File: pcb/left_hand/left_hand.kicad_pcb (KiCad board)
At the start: 2 copper layers, 150 x 105 mm, 43 parts, among them K0 SW_Push

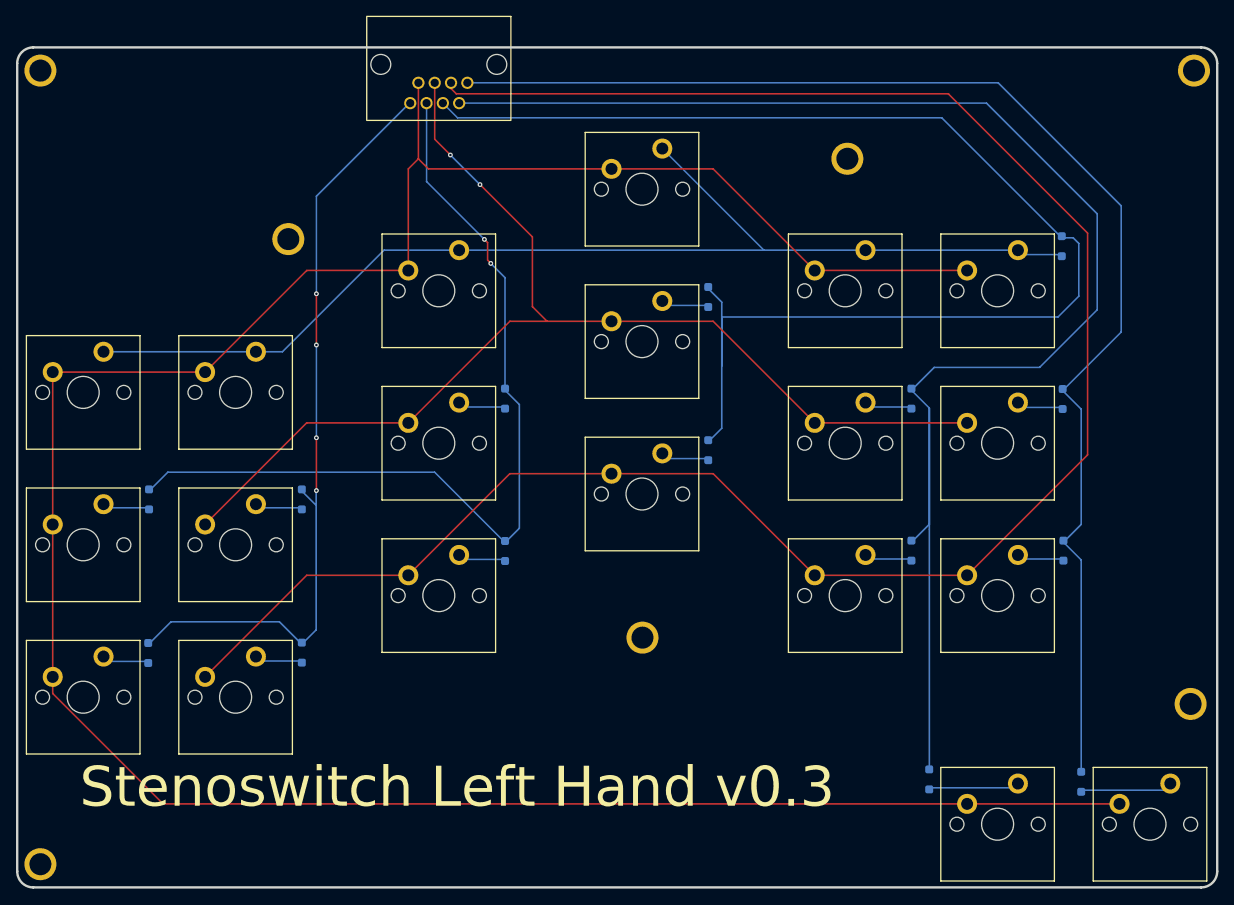
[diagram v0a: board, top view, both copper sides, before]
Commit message: Adjust left hand silkscreen; holes
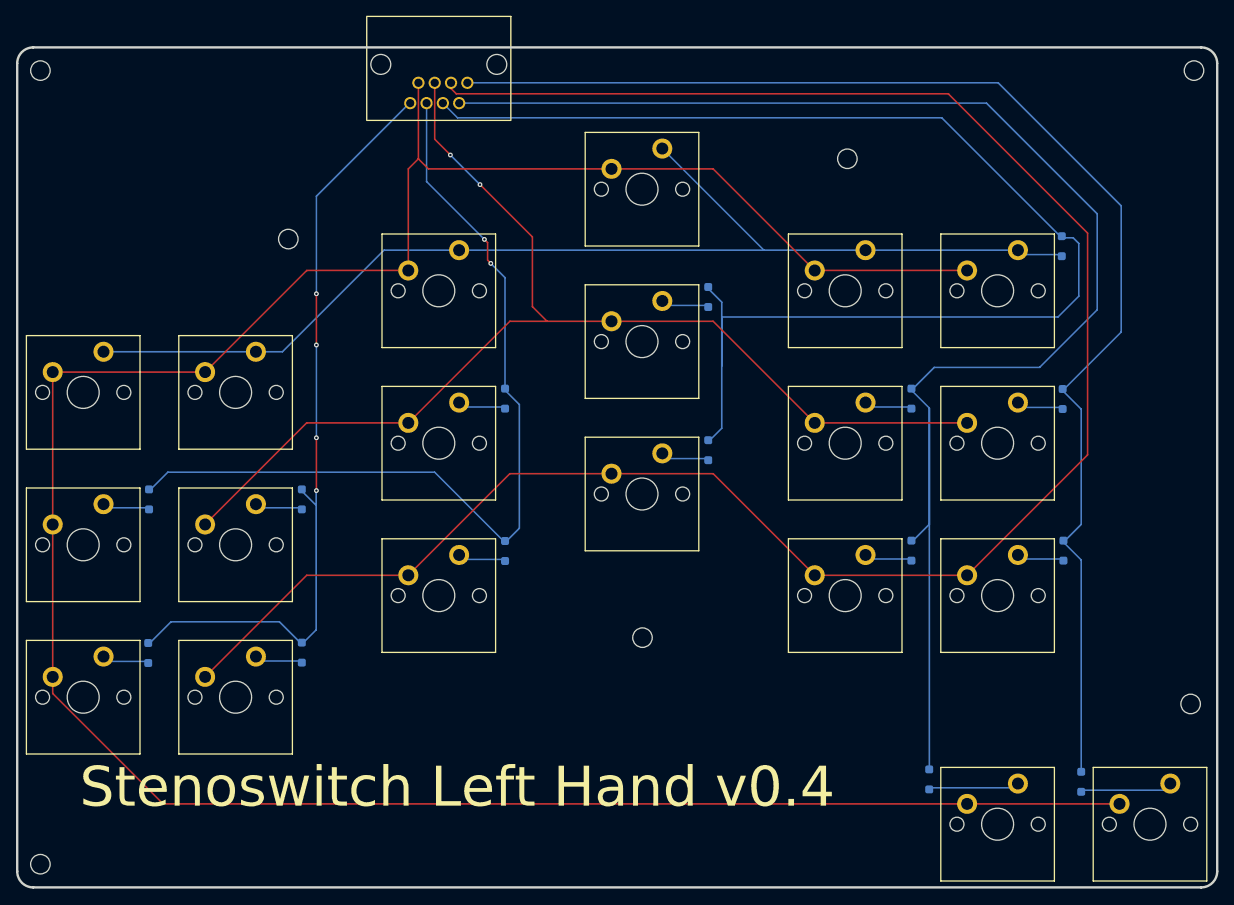
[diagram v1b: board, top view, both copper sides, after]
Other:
- board text added: "Stenoswitch Left Hand v0.4"
- board text removed: "Stenoswitch Left Hand v0.3"
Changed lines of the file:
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@@
 	(title_block
 		(title "Stenoswitch Left Hand")
-		(date "2025-10-20")
-		(rev "0.3")
+		(date "2025-11-14")
+		(rev "0.4")
 		(company "https://github.com/Bennett-Petzold/stenoswitch")
 		(comment 1 "NO WARRANTY. See license.")
@@
 			)
 		)
-		(pad "" thru_hole circle
+		(pad "" np_thru_hole circle
 			(at 0 0 180)
-			(size 4 4)
-			(drill 2.75)
+			(size 2.4384 2.4384)
+			(drill 2.4384)
 			(layers "*.Cu" "*.Mask")
-			(remove_unused_layers no)
 		)
 		(embedded_fonts no)
@@
 			)
 		)
-		(pad "" thru_hole circle
+		(pad "" np_thru_hole circle
 			(at 0 0 180)
-			(size 4 4)
-			(drill 2.75)
+			(size 2.4384 2.4384)
+			(drill 2.4384)
 			(layers "*.Cu" "*.Mask")
-			(remove_unused_layers no)
 		)
 		(embedded_fonts no)
@@
 			)
 		)
-		(pad "" thru_hole circle
+		(pad "" np_thru_hole circle
 			(at 0 0 180)
-			(size 4 4)
-			(drill 2.75)
+			(size 2.4384 2.4384)
+			(drill 2.4384)
 			(layers "*.Cu" "*.Mask")
-			(remove_unused_layers no)
 		)
 		(embedded_fonts no)
@@
 			)
 		)
-		(pad "" thru_hole circle
+		(pad "" np_thru_hole circle
 			(at 0 0 180)
-			(size 4 4)
-			(drill 2.75)
+			(size 2.4384 2.4384)
+			(drill 2.4384)
 			(layers "*.Cu" "*.Mask")
-			(remove_unused_layers no)
 		)
 		(embedded_fonts no)
@@
 			)
 		)
-		(pad "" thru_hole circle
+		(pad "" np_thru_hole circle
 			(at 0 0 180)
-			(size 4 4)
-			(drill 2.75)
+			(size 2.4384 2.4384)
+			(drill 2.4384)
 			(layers "*.Cu" "*.Mask")
-			(remove_unused_layers no)
 		)
 		(embedded_fonts no)
@@
 			)
 		)
-		(pad "" thru_hole circle
+		(pad "" np_thru_hole circle
 			(at 0 0 180)
-			(size 4 4)
-			(drill 2.75)
+			(size 2.4384 2.4384)
+			(drill 2.4384)
 			(layers "*.Cu" "*.Mask")
-			(remove_unused_layers no)
 		)
 		(embedded_fonts no)
@@
 			)
 		)
-		(pad "" thru_hole circle
+		(pad "" np_thru_hole circle
 			(at 0 0 180)
-			(size 4 4)
-			(drill 2.75)
+			(size 2.4384 2.4384)
+			(drill 2.4384)
 			(layers "*.Cu" "*.Mask")
-			(remove_unused_layers no)
 		)
 		(embedded_fonts no)
@@
 		(layer "Edge.Cuts")
 	)
-	(gr_text "Stenoswitch Left Hand v0.3"
+	(gr_text "Stenoswitch Left Hand v0.4"
 		(at 73.8 141.6 0)
 		(layer "F.SilkS")
@@
 	)
 	(gr_text "*"
-		(at 126.6 87.6 90)
+		(at 127.2 87.6 90)
 		(layer "B.SilkS")
 		(effects
@@
 		)
 	)
-	(gr_text "Stenoswitch Left Hand v0.3"
+	(gr_text "Stenoswitch Left Hand v0.4"
 		(at 179.2 148.8 0)
 		(layer "B.SilkS")
@@
 			(keep_text_aligned yes)
 		)
-		(gr_text "2.9"
+		(gr_text "0.1142"
 			(at 67.45 43.25 0)
 			(layer "Dwgs.User")
@@
 			(keep_text_aligned yes)
 		)
-		(gr_text "25.4"
+		(gr_text "1"
 			(at 131.4 123.25 0)
 			(layer "Dwgs.User")
@@
 			(keep_text_aligned yes)
 		)
-		(gr_text "25.4"
+		(gr_text "1"
 			(at 156.8 123.25 0)
 			(layer "Dwgs.User")
@@
 			(keep_text_aligned yes)
 		)
-		(gr_text "2.9"
+		(gr_text "0.1142"
 			(at 73.8 47.6 90)
 			(layer "Dwgs.User")
@@
 			(keep_text_aligned yes)
 		)
-		(gr_text "12.7"
+		(gr_text "0.5"
 			(at 131.52 108.375 90)
 			(layer "Dwgs.User")
@@
 			(keep_text_aligned yes)
 		)
-		(gr_text "105"
+		(gr_text "4.1339"
 			(at 224.8 98.5 90)
 			(layer "Dwgs.User")
@@
 			(keep_text_aligned yes)
 		)
-		(gr_text "12.7"
+		(gr_text "0.5"
 			(at 108.12 121.075 90)
 			(layer "Dwgs.User")
@@
 			(keep_text_aligned yes)
 		)
-		(gr_text "19.05"
+		(gr_text "0.75"
 			(at 179.025 123.25 0)
 			(layer "Dwgs.User")
@@
 			(keep_text_aligned yes)
 		)
-		(gr_text "19.05"
+		(gr_text "0.75"
 			(at 204.62 105.2 90)
 			(layer "Dwgs.User")
@@
 			(keep_text_aligned yes)
 		)
-		(gr_text "28.575"
+		(gr_text "1.125"
 			(at 187.4 129.0125 90)
 			(layer "Dwgs.User")
@@
 			(keep_text_aligned yes)
 		)
-		(gr_text "150"
+		(gr_text "5.9055"
 			(at 141 36.8 0)
 			(layer "Dwgs.User")
@@
 			(keep_text_aligned yes)
 		)
-		(gr_text "25.4"
+		(gr_text "1"
 			(at 106 126.275 0)
 			(layer "Dwgs.User")
@@
 			(keep_text_aligned yes)
 		)
-		(gr_text "12.7"
+		(gr_text "0.5"
 			(at 156.12 108.375 90)
 			(layer "Dwgs.User")
